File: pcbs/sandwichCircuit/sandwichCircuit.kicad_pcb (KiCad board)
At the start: 2 copper layers, 76 x 56 mm, 10 parts, among them IC1 3678, J5 Audio Out, U1 ESP32-DevKitC header, U2 CP2104 USB A board

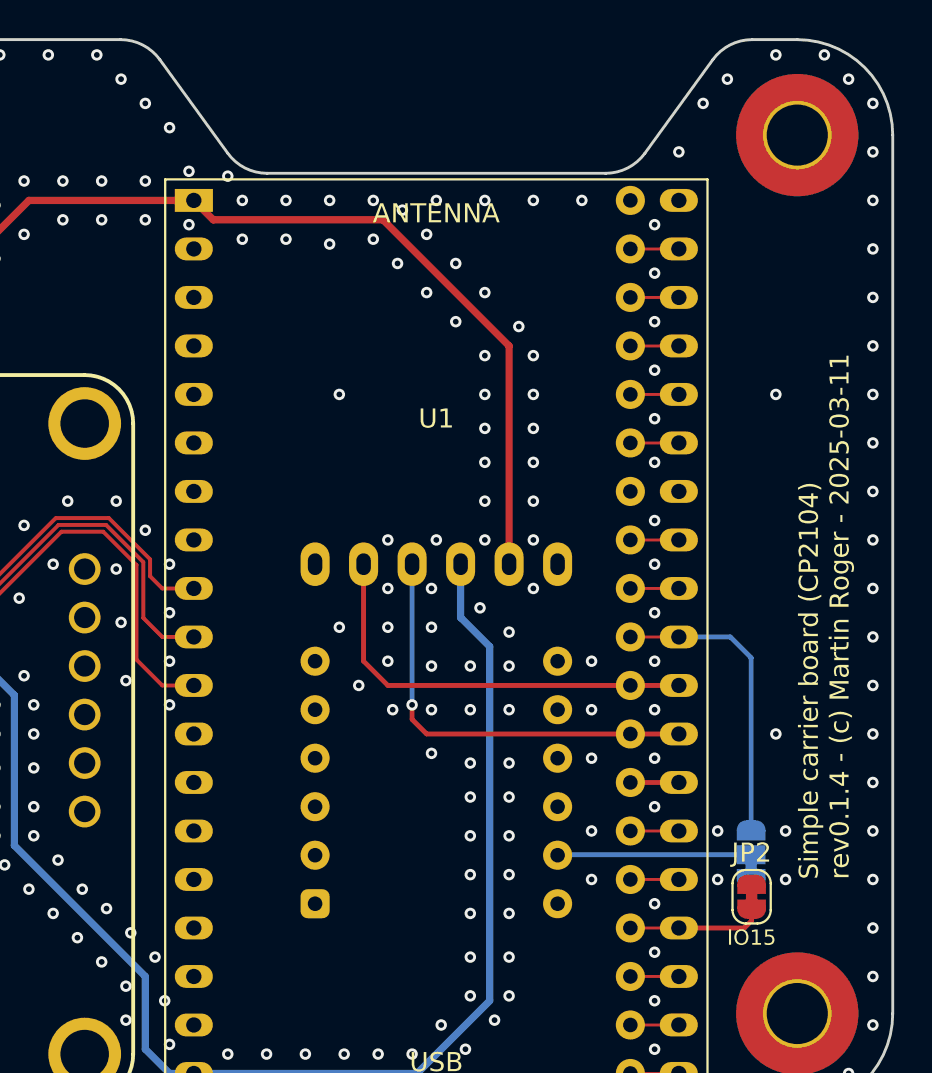
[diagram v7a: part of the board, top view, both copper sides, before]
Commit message: Update SCB
Updated SCB :
- Upper pins of CP2104 moved about 0.5mm up
- CP2104 reset is now available on GPIO 13
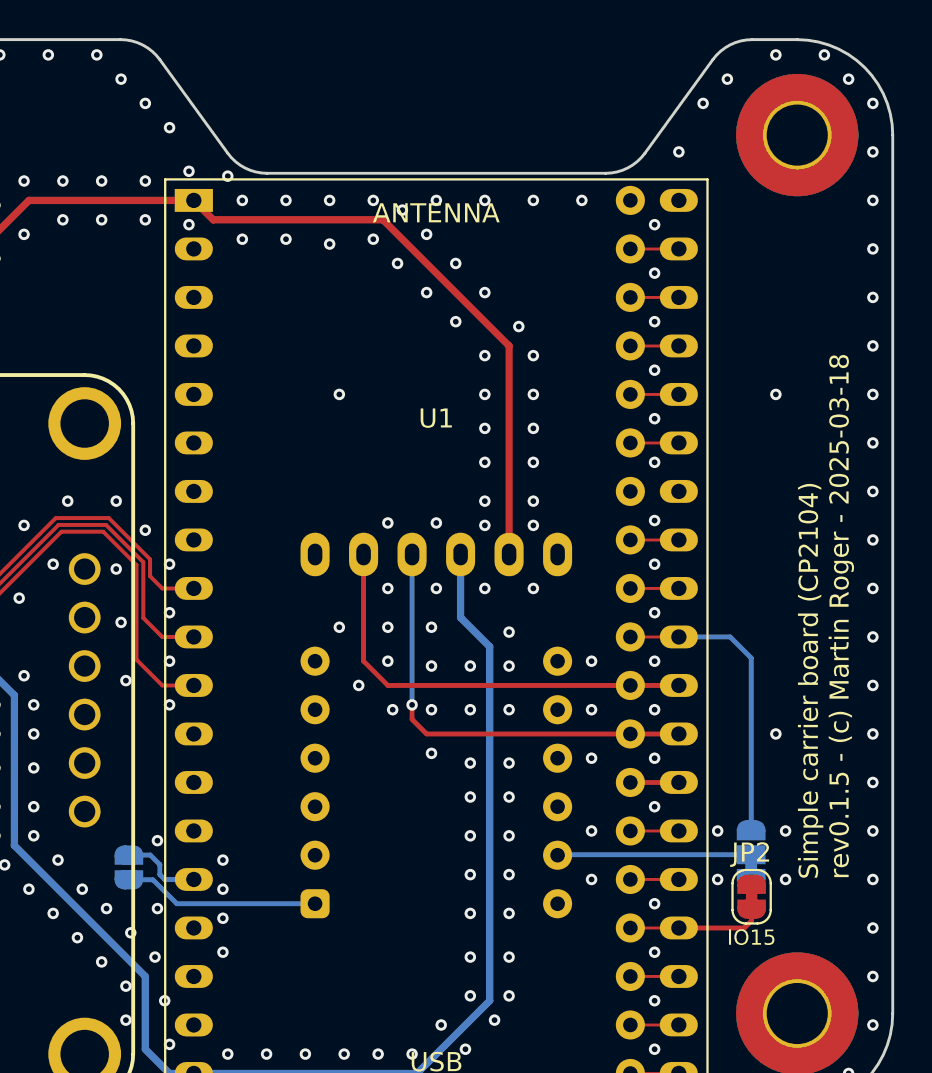
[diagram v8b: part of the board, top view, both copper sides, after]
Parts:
- added JP3: SolderJumper_2_Open, Jumper:SolderJumper-2_P1.3mm_Open_RoundedPad1.0x1.5mm, B.Cu at (149.0, 93.3)
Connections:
- U1 pad 15: unconnected-(U1-MTCK/GPIO13/ADC2_CH4-Pad15) -> GPIO13
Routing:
- net RST: track 0.00 -> 10.3 mm
- net GPIO13: track 0.00 -> 4.24 mm
- net GND: vias 310 -> 316
